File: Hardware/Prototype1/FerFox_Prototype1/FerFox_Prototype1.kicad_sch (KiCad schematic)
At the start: 36 parts, among them J1 Conn_01x08_Pin, J2 Conn_01x06_Pin, U1 STM32F401CCUx, U2 LY68L6400, Y1 25MHz, Y2 32768 Hz

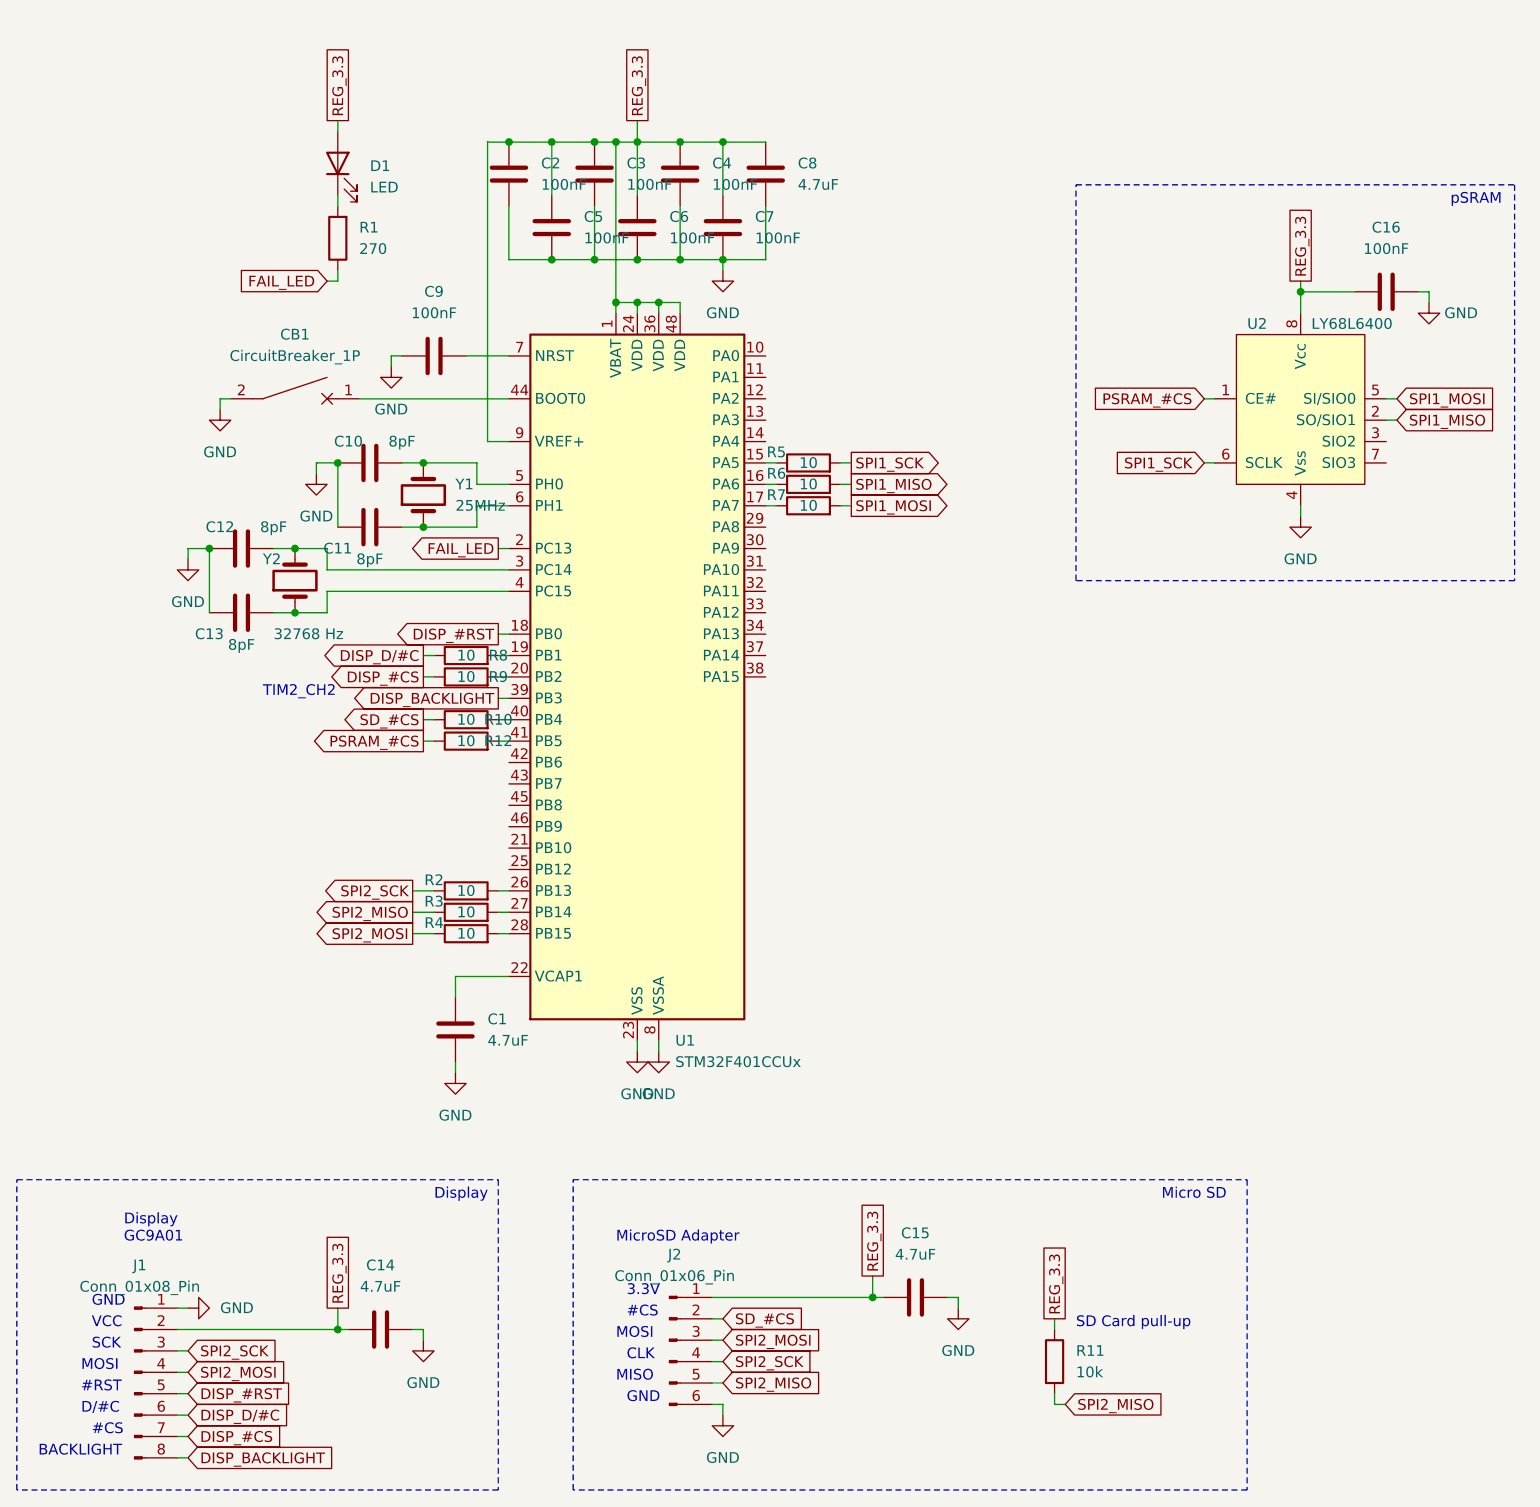
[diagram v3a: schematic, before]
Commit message: Working write/read (32 bytes packet) to/from LY68L6400
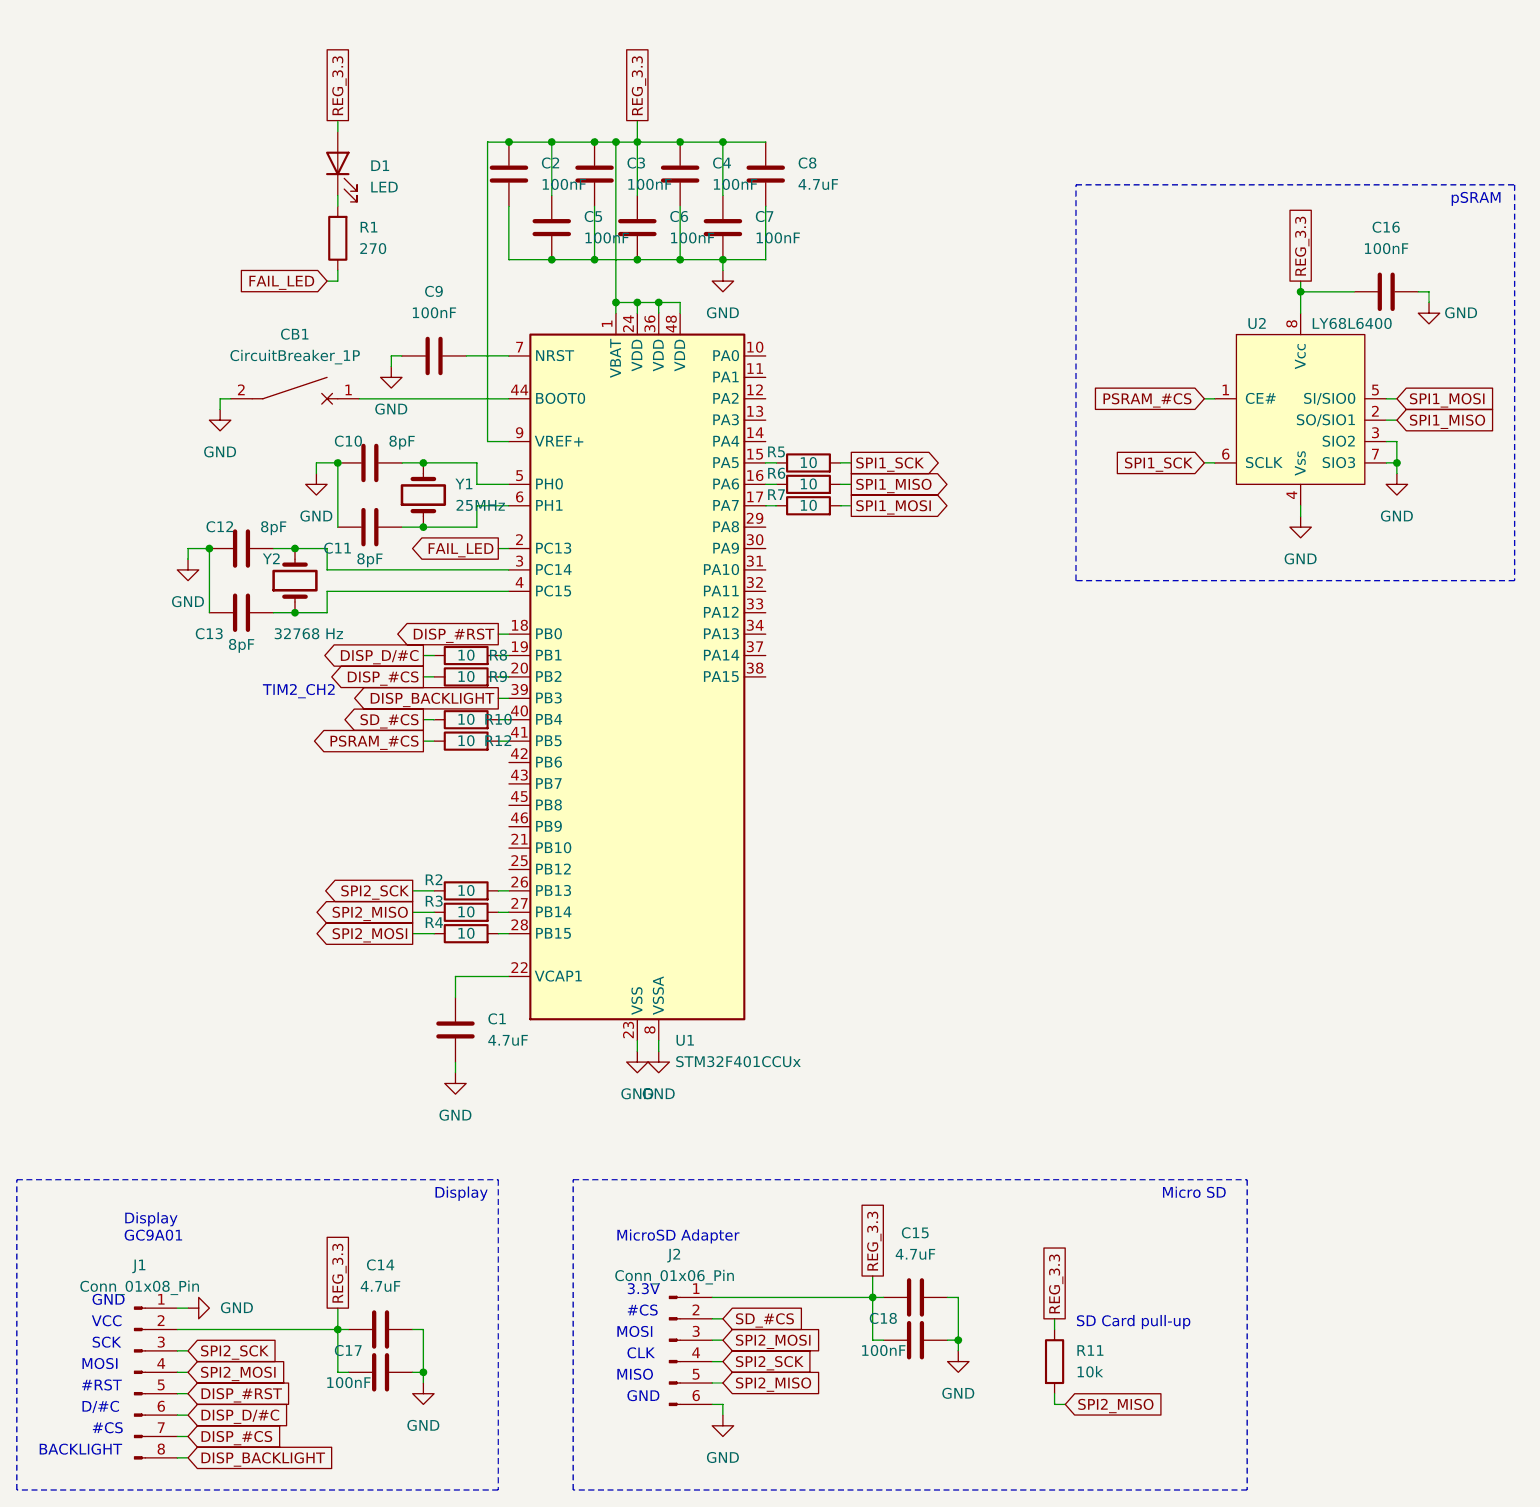
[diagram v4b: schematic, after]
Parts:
- added C17, C18: 100nF, symbol Device:C
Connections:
- net GND: now also U2.3 (SIO2), U2.7 (SIO3), C17.2, C18.2
- net REG_3.3: now also C17.1, C18.1
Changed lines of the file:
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@@
   (junction (at 185.42 73.66) (diameter 0) (color 0 0 0 0)
   )
+  (junction (at 311.15 73.66) (diameter 0) (color 0 0 0 0)
+  )
+  (junction (at 195.58 181.61) (diameter 0) (color 0 0 0 0)
+  )
   (junction (at 220.98 35.56) (diameter 0) (color 0 0 0 0)
   )
@@
   (junction (at 218.44 35.56) (diameter 0) (color 0 0 0 0)
   )
+  (junction (at 259.08 177.8) (diameter 0) (color 0 0 0 0)
+  )
   (junction (at 180.34 83.82) (diameter 0) (color 0 0 0 0)
   )
@@
     (stroke (width 0) (type default))
   )
-  (wire (pts (xy 259.08 173.99) (xy 259.08 172.72))
-    (stroke (width 0) (type default))
-  )
   (wire (pts (xy 187.96 66.04) (xy 205.74 66.04))
     (stroke (width 0) (type default))
@@
     (stroke (width 0) (type default))
   )
-  (wire (pts (xy 195.58 176.53) (xy 195.58 177.8))
+  (wire (pts (xy 195.58 176.53) (xy 195.58 181.61))
     (stroke (width 0) (type default))
   )
@@
     (stroke (width 0) (type default))
   )
+  (wire (pts (xy 195.58 181.61) (xy 194.31 181.61))
+    (stroke (width 0) (type default))
+  )
   (wire (pts (xy 195.58 96.52) (xy 196.85 96.52))
     (stroke (width 0) (type default))
   )
+  (wire (pts (xy 311.15 74.93) (xy 311.15 73.66))
+    (stroke (width 0) (type default))
+  )
   (wire (pts (xy 210.82 35.56) (xy 215.9 35.56))
     (stroke (width 0) (type default))
@@
     (stroke (width 0) (type default))
   )
+  (wire (pts (xy 259.08 172.72) (xy 257.81 172.72))
+    (stroke (width 0) (type default))
+  )
   (wire (pts (xy 226.06 35.56) (xy 231.14 35.56))
     (stroke (width 0) (type default))
@@
     (stroke (width 0) (type default))
   )
+  (wire (pts (xy 311.15 73.66) (xy 309.88 73.66))
+    (stroke (width 0) (type default))
+  )
   (wire (pts (xy 245.11 73.66) (xy 246.38 73.66))
     (stroke (width 0) (type default))
@@
     (stroke (width 0) (type default))
   )
+  (wire (pts (xy 311.15 71.12) (xy 309.88 71.12))
+    (stroke (width 0) (type default))
+  )
   (wire (pts (xy 220.98 35.56) (xy 220.98 41.91))
     (stroke (width 0) (type default))
@@
     (stroke (width 0) (type default))
   )
+  (wire (pts (xy 195.58 181.61) (xy 195.58 182.88))
+    (stroke (width 0) (type default))
+  )
   (wire (pts (xy 226.06 49.53) (xy 231.14 49.53))
     (stroke (width 0) (type default))
@@
     (stroke (width 0) (type default))
   )
+  (wire (pts (xy 250.19 177.8) (xy 248.92 177.8))
+    (stroke (width 0) (type default))
+  )
   (wire (pts (xy 215.9 49.53) (xy 220.98 49.53))
     (stroke (width 0) (type default))
@@
     (stroke (width 0) (type default))
   )
+  (wire (pts (xy 259.08 177.8) (xy 259.08 172.72))
+    (stroke (width 0) (type default))
+  )
   (wire (pts (xy 200.66 60.96) (xy 205.74 60.96))
     (stroke (width 0) (type default))
@@
     (stroke (width 0) (type default))
   )
+  (wire (pts (xy 259.08 179.07) (xy 259.08 177.8))
+    (stroke (width 0) (type default))
+  )
+  (wire (pts (xy 311.15 73.66) (xy 311.15 71.12))
+    (stroke (width 0) (type default))
+  )
   (wire (pts (xy 220.98 35.56) (xy 226.06 35.56))
     (stroke (width 0) (type default))
@@
     (stroke (width 0) (type default))
   )
-  (wire (pts (xy 259.08 172.72) (xy 257.81 172.72))
-    (stroke (width 0) (type default))
-  )
   (wire (pts (xy 231.14 49.53) (xy 236.22 49.53))
     (stroke (width 0) (type default))
   )
+  (wire (pts (xy 257.81 177.8) (xy 259.08 177.8))
+    (stroke (width 0) (type default))
+  )
   (wire (pts (xy 166.37 186.69) (xy 167.64 186.69))
     (stroke (width 0) (type default))
@@
     (stroke (width 0) (type default))
   )
+  (wire (pts (xy 248.92 172.72) (xy 248.92 177.8))
+    (stroke (width 0) (type default))
+  )
   (wire (pts (xy 184.15 91.44) (xy 180.34 91.44))
     (stroke (width 0) (type default))
@@
     (stroke (width 0) (type default))
   )
+  (wire (pts (xy 185.42 176.53) (xy 185.42 181.61))
+    (stroke (width 0) (type default))
+  )
   (wire (pts (xy 191.77 60.96) (xy 193.04 60.96))
     (stroke (width 0) (type default))
@@
   )
   (wire (pts (xy 194.31 124.46) (xy 196.85 124.46))
+    (stroke (width 0) (type default))
+  )
+  (wire (pts (xy 186.69 181.61) (xy 185.42 181.61))
     (stroke (width 0) (type default))
   )
@@
     )
   )
-  (symbol (lib_id "power:GND") (at 259.08 173.99 0) (unit 1)
-    (in_bom yes) (on_board yes) (dnp no) (fields_autoplaced)
-    (property "Reference" "#PWR012" (at 259.08 180.34 0)
-      (effects (font (size 1.27 1.27)) hide)
-    )
-    (property "Value" "GND" (at 259.08 179.07 0)
-      (effects (font (size 1.27 1.27)))
-    )
-    (property "Footprint" "" (at 259.08 173.99 0)
-      (effects (font (size 1.27 1.27)) hide)
-    )
-    (property "Datasheet" "" (at 259.08 173.99 0)
+  (symbol (lib_id "power:GND") (at 259.08 179.07 0) (unit 1)
+    (in_bom yes) (on_board yes) (dnp no) (fields_autoplaced)
+    (property "Reference" "#PWR012" (at 259.08 185.42 0)
+      (effects (font (size 1.27 1.27)) hide)
+    )
+    (property "Value" "GND" (at 259.08 184.15 0)
+      (effects (font (size 1.27 1.27)))
+    )
+    (property "Footprint" "" (at 259.08 179.07 0)
+      (effects (font (size 1.27 1.27)) hide)
+    )
+    (property "Datasheet" "" (at 259.08 179.07 0)
       (effects (font (size 1.27 1.27)) hide)
     )
@@
     )
   )
-  (symbol (lib_id "power:GND") (at 195.58 177.8 0) (unit 1)
-    (in_bom yes) (on_board yes) (dnp no) (fields_autoplaced)
-    (property "Reference" "#PWR010" (at 195.58 184.15 0)
-      (effects (font (size 1.27 1.27)) hide)
-    )
-    (property "Value" "GND" (at 195.58 182.88 0)
-      (effects (font (size 1.27 1.27)))
-    )
-    (property "Footprint" "" (at 195.58 177.8 0)
-      (effects (font (size 1.27 1.27)) hide)
-    )
-    (property "Datasheet" "" (at 195.58 177.8 0)
+  (symbol (lib_id "power:GND") (at 195.58 182.88 0) (unit 1)
+    (in_bom yes) (on_board yes) (dnp no) (fields_autoplaced)
+    (property "Reference" "#PWR010" (at 195.58 189.23 0)
+      (effects (font (size 1.27 1.27)) hide)
+    )
+    (property "Value" "GND" (at 195.58 187.96 0)
+      (effects (font (size 1.27 1.27)))
+    )
+    (property "Footprint" "" (at 195.58 182.88 0)
+      (effects (font (size 1.27 1.27)) hide)
+    )
+    (property "Datasheet" "" (at 195.58 182.88 0)
       (effects (font (size 1.27 1.27)) hide)
     )
@@
     )
   )
+  (symbol (lib_id "power:GND") (at 311.15 74.93 0) (unit 1)
+    (in_bom yes) (on_board yes) (dnp no) (fields_autoplaced)
+    (property "Reference" "#PWR015" (at 311.15 81.28 0)
+      (effects (font (size 1.27 1.27)) hide)
+    )
+    (property "Value" "GND" (at 311.15 80.01 0)
+      (effects (font (size 1.27 1.27)))
+    )
+    (property "Footprint" "" (at 311.15 74.93 0)
+      (effects (font (size 1.27 1.27)) hide)
+    )
+    (property "Datasheet" "" (at 311.15 74.93 0)
+      (effects (font (size 1.27 1.27)) hide)
+    )
+    (pin "1")
+    (instances
+      (project "FerFox_Prototype1"
+        (path "/011f2c64-cf22-44cd-a30f-ff566a75b03a"
+          (reference "#PWR015") (unit 1)
+        )
+      )
+    )
+  )
   (symbol (lib_id "Device:C") (at 210.82 45.72 0) (unit 1)
     (in_bom yes) (on_board yes) (dnp no) (fields_autoplaced)
@@
     )
   )
+  (symbol (lib_id "Device:C") (at 190.5 181.61 90) (unit 1)
+    (in_bom yes) (on_board yes) (dnp no)
+    (property "Reference" "C17" (at 186.69 179.07 90)
+      (effects (font (size 1.27 1.27)))
+    )
+    (property "Value" "100nF" (at 186.69 182.88 90)
+      (effects (font (size 1.27 1.27)))
+    )
+    (property "Footprint" "" (at 194.31 180.6448 0)
+      (effects (font (size 1.27 1.27)) hide)
+    )
+    (property "Datasheet" "~" (at 190.5 181.61 0)
+      (effects (font (size 1.27 1.27)) hide)
+    )
+    (pin "1")
+    (pin "2")
+    (instances
+      (project "FerFox_Prototype1"
+        (path "/011f2c64-cf22-44cd-a30f-ff566a75b03a"
+          (reference "C17") (unit 1)
+        )
+      )
+    )
+  )
   (symbol (lib_id "power:GND") (at 223.52 143.51 0) (unit 1)
     (in_bom yes) (on_board yes) (dnp no) (fields_autoplaced)
@@
         )
       )
+    )
+  )
+  (symbol (lib_id "Device:C") (at 254 177.8 90) (unit 1)
+    (in_bom yes) (on_board yes) (dnp no)
+    (property "Reference" "C18" (at 250.19 175.26 90)
+      (effects (font (size 1.27 1.27)))
+    )
+    (property "Value" "100nF" (at 250.19 179.07 90)
+      (effects (font (size 1.27 1.27)))
+    )
+    (property "Footprint" "" (at 257.81 176.8348 0)
+      (effects (font (size 1.27 1.27)) hide)
+    )
+    (property "Datasheet" "~" (at 254 177.8 0)
+      (effects (font (size 1.27 1.27)) hide)
+    )
+    (pin "1")
+    (pin "2")
+    (instances
+      (project "FerFox_Prototype1"
+        (path "/011f2c64-cf22-44cd-a30f-ff566a75b03a"
+          (reference "C18") (unit 1)
+        )
+      )

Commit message: 2x faster SRAM bus
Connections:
- net SPI1_MISO: now also J2.5 (Pin_5), R11.2; no longer U2.2 (SO/SIO1)
- net SPI1_MOSI: now also J1.4 (Pin_4), J2.3 (Pin_3); no longer U2.5 (SI/SIO0)
- net SPI1_SCK: now also J1.3 (Pin_3), J2.4 (Pin_4); no longer U2.6 (SCLK)
- net SPI2_MISO: now also U2.2 (SO/SIO1); no longer J2.5 (Pin_5), R11.2
- net SPI2_MOSI: now also U2.5 (SI/SIO0); no longer J1.4 (Pin_4), J2.3 (Pin_3)
- net SPI2_SCK: now also U2.6 (SCLK); no longer J1.3 (Pin_3), J2.4 (Pin_4)
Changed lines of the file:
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@@
     )
   )
-  (global_label "SPI2_MOSI" (shape input) (at 167.64 181.61 0) (fields_autoplaced)
+  (global_label "SPI1_MOSI" (shape input) (at 167.64 181.61 0) (fields_autoplaced)
     (effects (font (size 1.27 1.27)) (justify left))
-    (property "Intersheetrefs" "${INTERSHEET_REFS}" (at 180.4034 181.61 0)
+    (property "Intersheetrefs" "${INTERSHEET_REFS}" (at 180.4828 181.61 0)
       (effects (font (size 1.27 1.27)) (justify left) hide)
     )
   )
-  (global_label "SPI2_MISO" (shape input) (at 231.14 182.88 0) (fields_autoplaced)
+  (global_label "SPI1_MISO" (shape input) (at 231.14 182.88 0) (fields_autoplaced)
     (effects (font (size 1.27 1.27)) (justify left))
-    (property "Intersheetrefs" "${INTERSHEET_REFS}" (at 243.9034 182.88 0)
+    (property "Intersheetrefs" "${INTERSHEET_REFS}" (at 243.9828 182.88 0)
       (effects (font (size 1.27 1.27)) (justify left) hide)
     )
@@
     )
   )
-  (global_label "SPI2_SCK" (shape input) (at 231.14 180.34 0) (fields_autoplaced)
+  (global_label "SPI1_SCK" (shape input) (at 231.14 180.34 0) (fields_autoplaced)
     (effects (font (size 1.27 1.27)) (justify left))
-    (property "Intersheetrefs" "${INTERSHEET_REFS}" (at 243.0567 180.34 0)
+    (property "Intersheetrefs" "${INTERSHEET_REFS}" (at 243.1361 180.34 0)
       (effects (font (size 1.27 1.27)) (justify left) hide)
     )
@@
     )
   )
-  (global_label "SPI1_MOSI" (shape input) (at 311.15 66.04 0) (fields_autoplaced)
+  (global_label "SPI2_MOSI" (shape input) (at 311.15 66.04 0) (fields_autoplaced)
     (effects (font (size 1.27 1.27)) (justify left))
     (property "Intersheetrefs" "${INTERSHEET_REFS}" (at 323.9928 66.04 0)
@@
     )
   )
-  (global_label "SPI1_MISO" (shape input) (at 311.15 68.58 0) (fields_autoplaced)
+  (global_label "SPI2_MISO" (shape input) (at 311.15 68.58 0) (fields_autoplaced)
     (effects (font (size 1.27 1.27)) (justify left))
     (property "Intersheetrefs" "${INTERSHEET_REFS}" (at 323.9928 68.58 0)
@@
     )
   )
-  (global_label "SPI1_SCK" (shape input) (at 288.29 73.66 180) (fields_autoplaced)
+  (global_label "SPI2_SCK" (shape input) (at 288.29 73.66 180) (fields_autoplaced)
     (effects (font (size 1.27 1.27)) (justify right))
     (property "Intersheetrefs" "${INTERSHEET_REFS}" (at 276.2939 73.66 0)
@@
     )
   )
-  (global_label "SPI2_MOSI" (shape input) (at 231.14 177.8 0) (fields_autoplaced)
+  (global_label "SPI1_MOSI" (shape input) (at 231.14 177.8 0) (fields_autoplaced)
     (effects (font (size 1.27 1.27)) (justify left))
-    (property "Intersheetrefs" "${INTERSHEET_REFS}" (at 243.9034 177.8 0)
+    (property "Intersheetrefs" "${INTERSHEET_REFS}" (at 243.9828 177.8 0)
       (effects (font (size 1.27 1.27)) (justify left) hide)
     )
   )
-  (global_label "SPI2_SCK" (shape input) (at 167.64 179.07 0) (fields_autoplaced)
+  (global_label "SPI1_SCK" (shape input) (at 167.64 179.07 0) (fields_autoplaced)
     (effects (font (size 1.27 1.27)) (justify left))
-    (property "Intersheetrefs" "${INTERSHEET_REFS}" (at 179.5567 179.07 0)
+    (property "Intersheetrefs" "${INTERSHEET_REFS}" (at 179.6361 179.07 0)
       (effects (font (size 1.27 1.27)) (justify left) hide)
     )
@@
     )
   )
-  (global_label "SPI2_MISO" (shape input) (at 271.78 185.42 0) (fields_autoplaced)
+  (global_label "SPI1_MISO" (shape input) (at 271.78 185.42 0) (fields_autoplaced)
     (effects (font (size 1.27 1.27)) (justify left))
-    (property "Intersheetrefs" "${INTERSHEET_REFS}" (at 284.5434 185.42 0)
+    (property "Intersheetrefs" "${INTERSHEET_REFS}" (at 284.6228 185.42 0)
       (effects (font (size 1.27 1.27)) (justify left) hide)
     )
